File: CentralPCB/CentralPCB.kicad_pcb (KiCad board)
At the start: 2 copper layers, 56 parts, among them J1 POWER HEADER, J2 SPI Header, J3 Conn_02x16_Odd_Even, J4 Conn_Coaxial, J5 Conn_02x10_Odd_Even, J6 Conn_01x05, U1 AD8531, U2 Teensy4.1, U3 BA7810CP-E2

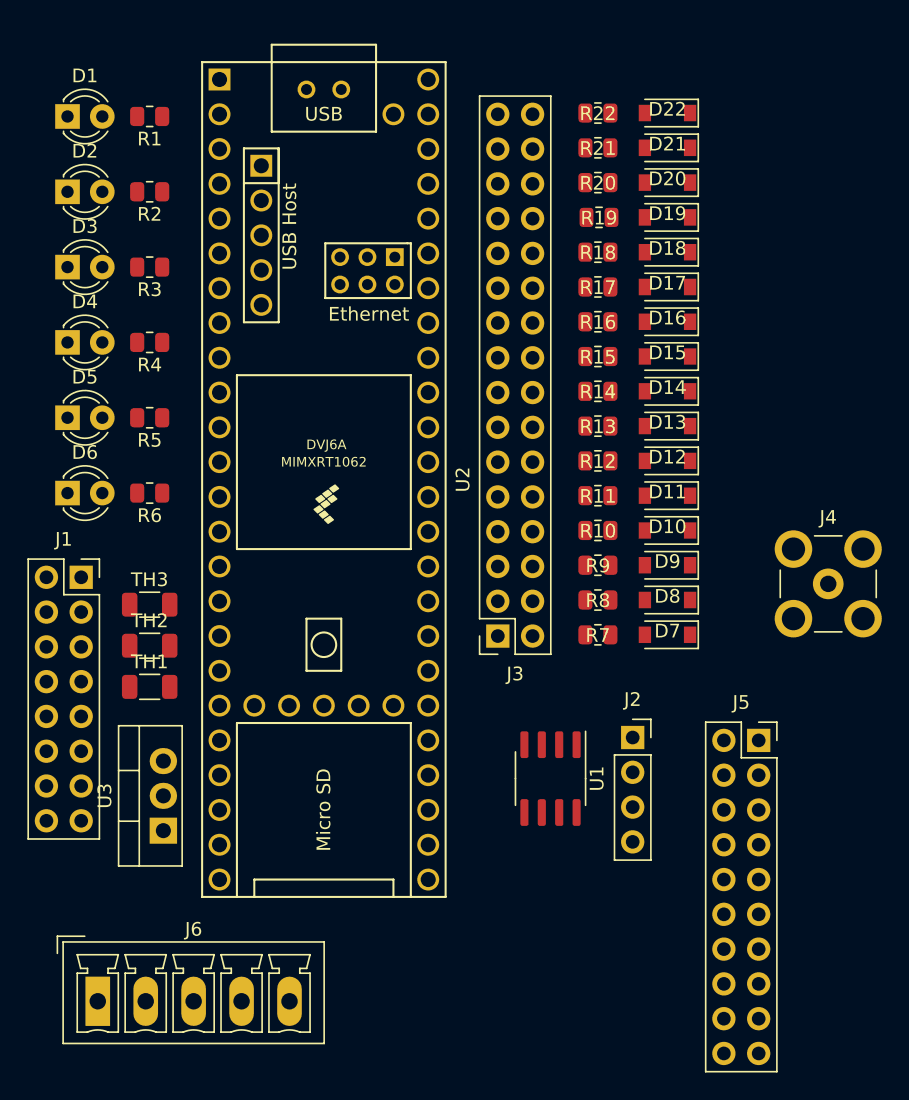
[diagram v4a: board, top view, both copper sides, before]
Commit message: Changed phoenix connector
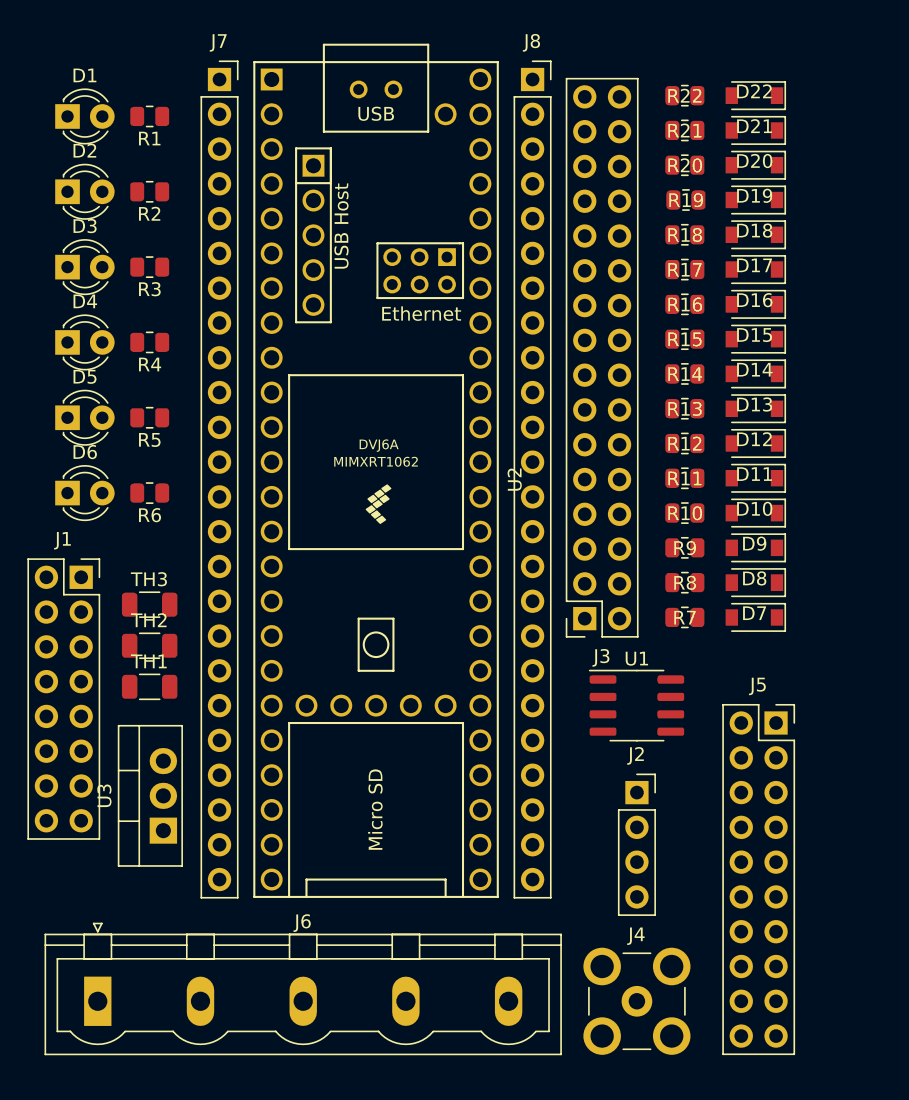
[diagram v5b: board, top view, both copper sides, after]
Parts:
- added J7: Conn_01x24, Connector_PinSocket_2.54mm:PinSocket_1x24_P2.54mm_Vertical, F.Cu at (27.9, 13.9)
- added J8: Conn_01x24, Connector_PinSocket_2.54mm:PinSocket_1x24_P2.54mm_Vertical, F.Cu at (50.7, 13.9)
- J6: footprint Connectors_Phoenix:PhoenixContact_MCV-G_05x3.50mm_Vertical -> Connectors_Phoenix:PhoenixContact_GMSTBVA-G_05x7.50mm_Vertical
- moved J4 33.5 mm to (58.4, 81.2)
- moved U1 8.26 mm to (58.4, 59.6), turned to 0 degrees
- moved R10 6.48 mm to (61.9, 45.6)
- moved R14 6.48 mm to (61.9, 35.4)
- moved R15 6.48 mm to (61.9, 32.9)
- moved R16 6.48 mm to (61.9, 30.3)
- moved R17 6.48 mm to (61.9, 27.8)
- moved R18 6.48 mm to (61.9, 25.2)
- moved R20 6.48 mm to (61.9, 20.2)
- moved R21 6.48 mm to (61.9, 17.6)
- moved R22 6.48 mm to (61.9, 15.1)
- moved R7 6.48 mm to (61.9, 53.2)
- moved R8 6.48 mm to (61.9, 50.6)
- moved R9 6.48 mm to (61.9, 48.1)
- moved R11 6.48 mm to (61.9, 43.0)
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
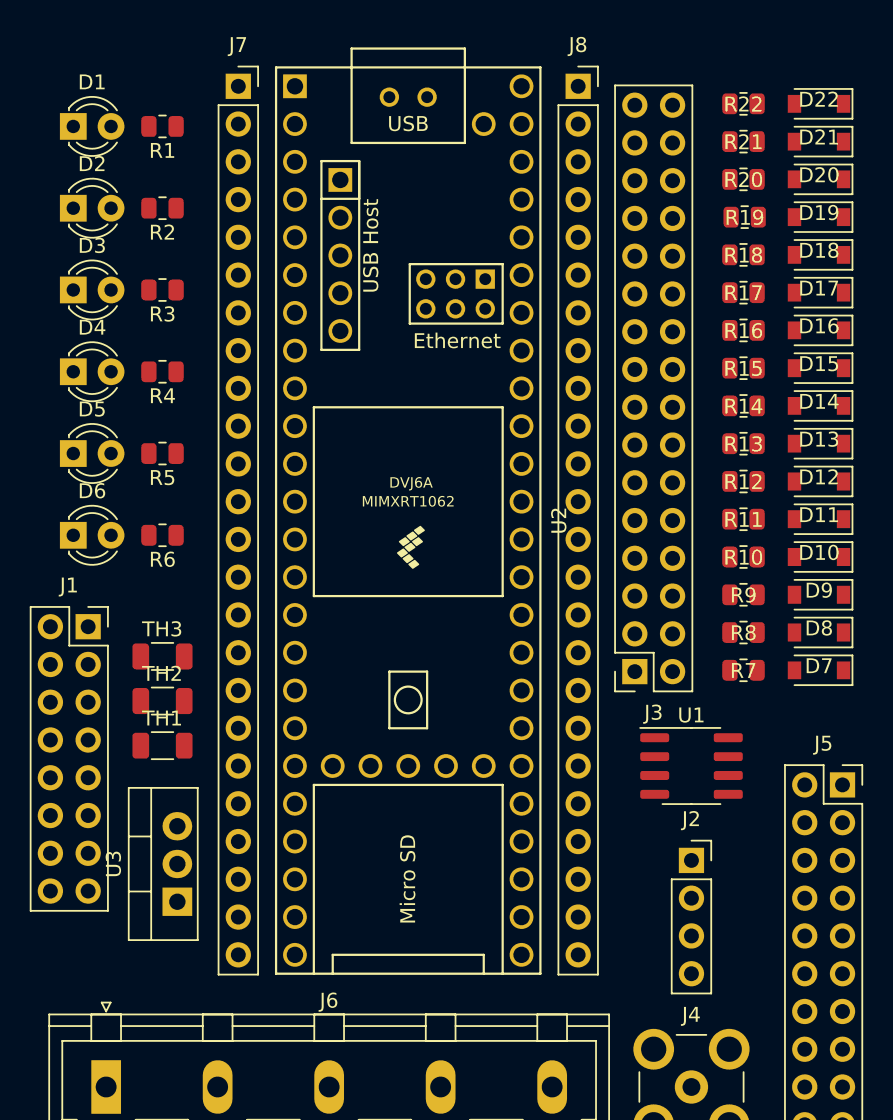
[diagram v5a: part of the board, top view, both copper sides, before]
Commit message: -12v LED
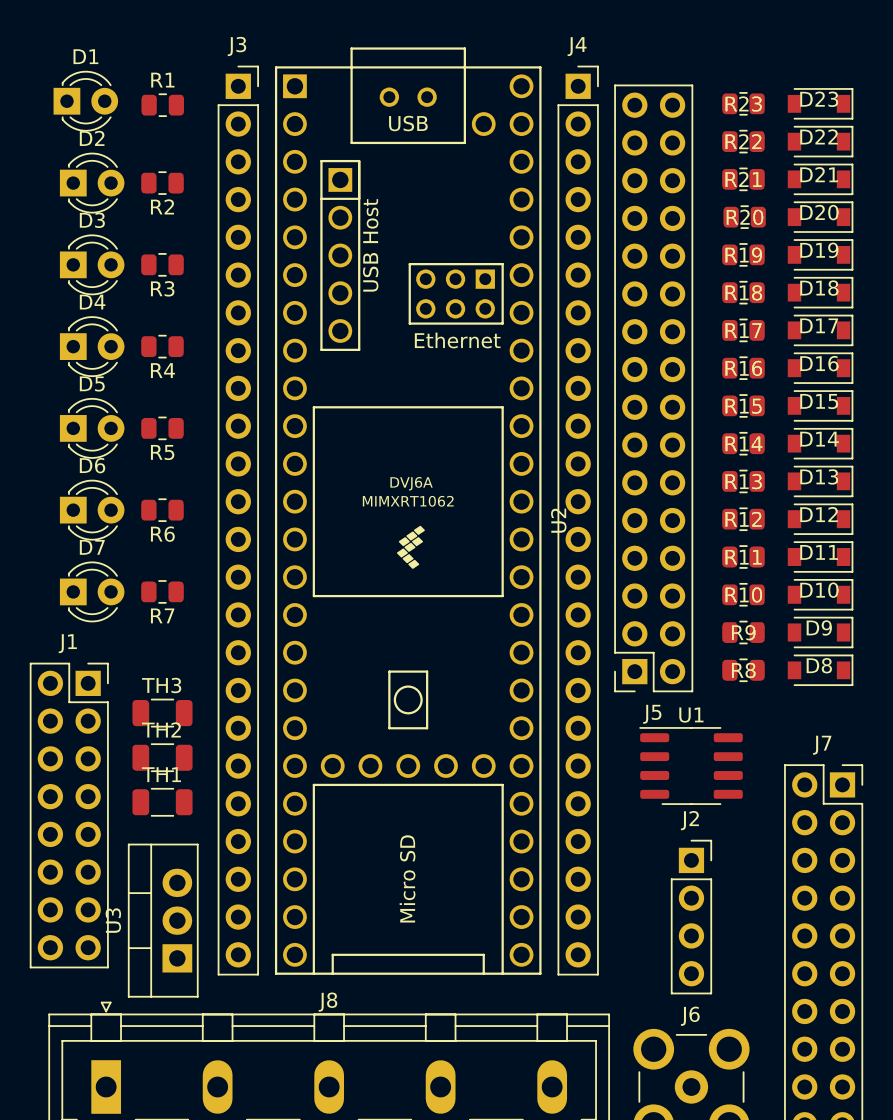
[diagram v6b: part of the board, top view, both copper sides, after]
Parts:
- added D1: 12V_POW, LED_THT:LED_D3.0mm, F.Cu at (16.4, 14.9)
- added R1: ?, Resistor_SMD:R_0805_2012Metric, F.Cu at (22.8, 15.2)
- moved D2 3.81 mm to (16.8, 20.4)
- moved D3 3.81 mm to (16.8, 25.9)
- moved D4 3.81 mm to (16.8, 31.4)
- moved D5 3.81 mm to (16.8, 36.9)
- moved D6 3.81 mm to (16.8, 42.4)
- moved D7 3.81 mm to (16.8, 47.9)
- moved J1 3.81 mm to (17.8, 54.1)
- moved R2 3.81 mm to (22.8, 20.4)
- moved R3 3.81 mm to (22.8, 25.9)
- moved R4 3.81 mm to (22.8, 31.4)
- moved R5 3.81 mm to (22.8, 36.9)
- moved R6 3.81 mm to (22.8, 42.4)
- moved R7 3.81 mm to (22.8, 47.9)
- moved TH1 3.81 mm to (22.8, 62.1)
- moved TH2 3.81 mm to (22.8, 59.1)
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- renumbered D9 to D10, D10 to D11, D11 to D12, D12 to D13, D13 to D14, D14 to D15, D15 to D16, D16 to D17, D17 to D18, D18 to D19, D1 to D2, D19 to D20, D20 to D21, D21 to D22, D22 to D23, D2 to D3, D3 to D4, D4 to D5, D5 to D6, D6 to D7, D7 to D8, D8 to D9, J7 to J3, J8 to J4, J3 to J5, J4 to J6, J5 to J7, J6 to J8, R9 to R10, R10 to R11, R11 to R12, R12 to R13, R13 to R14, R14 to R15, R15 to R16, R16 to R17, R17 to R18, R18 to R19, R1 to R2, R19 to R20, R20 to R21, R21 to R22, R22 to R23, R2 to R3, R3 to R4, R4 to R5, R5 to R6, R6 to R7, R7 to R8, R8 to R9

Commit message: Began CentralPCB layout
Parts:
- moved R1 140.6 mm to (88.8, 139.3), turned to 180 degrees
- moved D1 139.8 mm to (80.3, 139.3)
- moved R3 122.0 mm to (88.8, 128.5)
- moved D3 120.7 mm to (80.3, 128.5)
- moved D11 116.7 mm to (140.1, 136.5), turned to 0 degrees
- moved D16 116.7 mm to (140.1, 123.8), turned to 0 degrees
- moved D8 116.7 mm to (140.1, 144.1), turned to 0 degrees
- moved D10 116.7 mm to (140.1, 139.0), turned to 0 degrees
- moved D14 116.7 mm to (140.1, 128.9), turned to 0 degrees
- moved D15 116.7 mm to (140.1, 126.3), turned to 0 degrees
- moved D17 116.7 mm to (140.1, 121.3), turned to 0 degrees
- moved D19 116.7 mm to (140.1, 116.2), turned to 0 degrees
- moved D21 116.7 mm to (140.1, 111.1), turned to 0 degrees
- moved D22 116.7 mm to (140.1, 108.6), turned to 0 degrees
- moved D23 116.7 mm to (140.1, 106.0), turned to 0 degrees
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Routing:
- net +5V: track 0.00 -> 210.8 mm
- net DC4: track 0.00 -> 82.2 mm, vias 0 -> 1
- net DC3: track 0.00 -> 78.1 mm, vias 0 -> 1
- net +12V: track 0.00 -> 71.9 mm, vias 0 -> 4
- net DC2: track 0.00 -> 71.1 mm, vias 0 -> 1
- net GND: track 0.00 -> 66.4 mm, vias 0 -> 4
- net -12V: track 0.00 -> 62.0 mm
- net DC1: track 0.00 -> 57.2 mm
- net RESET: track 0.00 -> 44.3 mm, vias 0 -> 2
- net +10V: track 0.00 -> 42.9 mm
- net LDAC: track 0.00 -> 42.1 mm
- net CLR: track 0.00 -> 42.1 mm
- net DB4: track 0.00 -> 35.5 mm, vias 0 -> 1
- net DB3: track 0.00 -> 35.5 mm, vias 0 -> 1
- net DB2: track 0.00 -> 35.5 mm, vias 0 -> 1
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- added copper zone on F.Cu, net GND
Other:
- board outline added: 71.1 x 76.2 mm
- net class Default: clearance 0.2 -> 0.1778; trace_width 0.25 -> 0.1778; via_dia 0.8 -> 0.6858; via_drill 0.4 -> 0.3302
- rule trace_clearance: 0.2 -> 0.1778
- rule trace_min: 0.2 -> 0.1524
- rule via_min_drill: 0.3 -> 0.254
- rule via_min_size: 0.4 -> 0.508

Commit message: More routing CentralPCB
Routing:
- net Net-(J4-Pad3): track 3.81 -> 81.6 mm, vias 0 -> 2
- net +3V3: track 5.48 -> 83.0 mm, vias 0 -> 2
- net +12V: track 71.9 -> 149.2 mm, vias 4 -> 5
- net MOSI0: track 22.8 -> 89.7 mm, vias 0 -> 1
- net DD4: track 8.11 -> 72.1 mm, vias 0 -> 2
- net DD2: track 8.11 -> 72.1 mm, vias 0 -> 2
- net DD1: track 8.03 -> 71.5 mm, vias 0 -> 2
- net DD3: track 8.11 -> 70.5 mm, vias 0 -> 2
- net MISO0: track 3.81 -> 55.7 mm, vias 0 -> 2
- net CS0: track 15.9 -> 66.4 mm, vias 0 -> 3
- net GND: track 66.4 -> 94.7 mm, vias 4 -> 19
- net SCK0: track 16.9 -> 42.1 mm, vias 0 -> 1
- added copper zone on B.Cu, net GND
